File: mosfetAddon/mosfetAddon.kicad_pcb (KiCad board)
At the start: 2 copper layers, 89 x 61 mm, 70 parts, among them J1 coil, J10 Conn_01x18_Male, J2 coil, J3 coil, J4 coil, J5 coil, J6 coil, J7 coil, J8 coil, J9 pow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

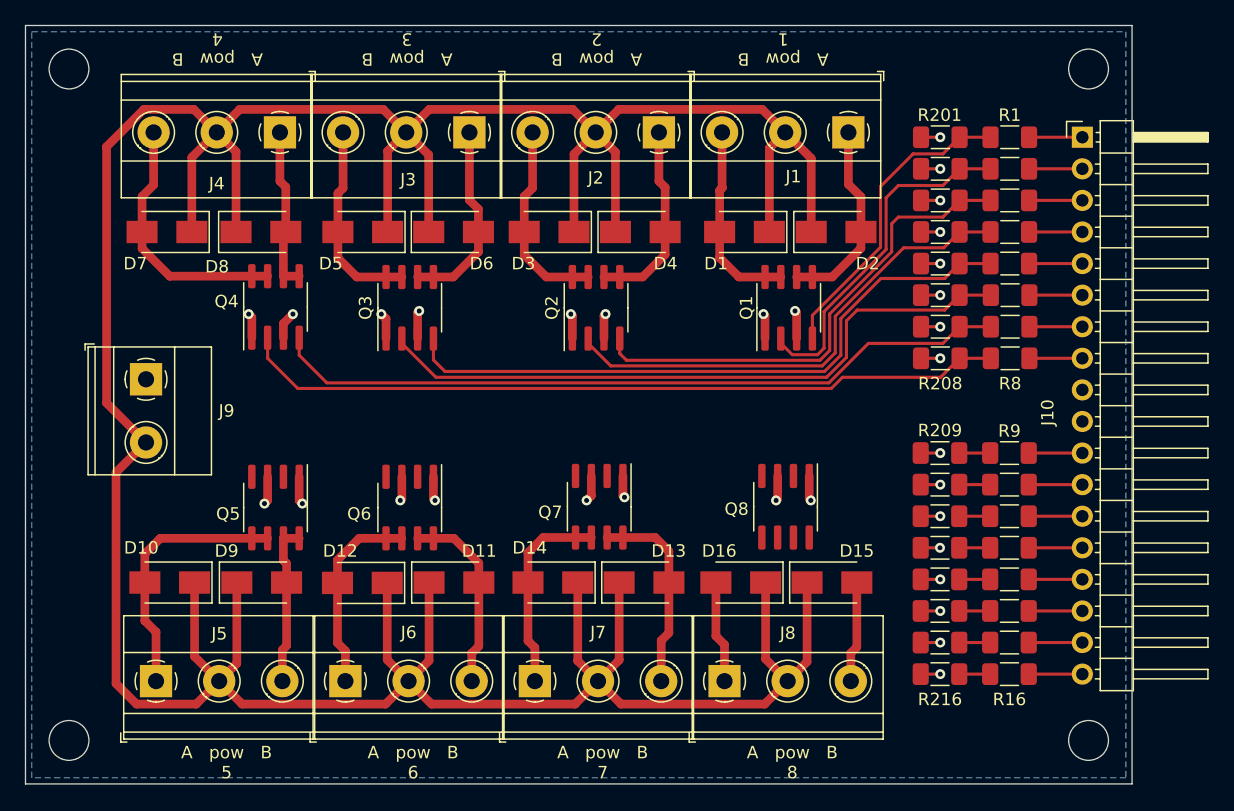
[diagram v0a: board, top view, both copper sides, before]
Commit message: relay are working but one. Multimaus control with IO sometimes seem buggy, but works in general. In worst case you have to press the same button another time.
Storing and saving program also works. Only the channel selection does not seem to work properly.
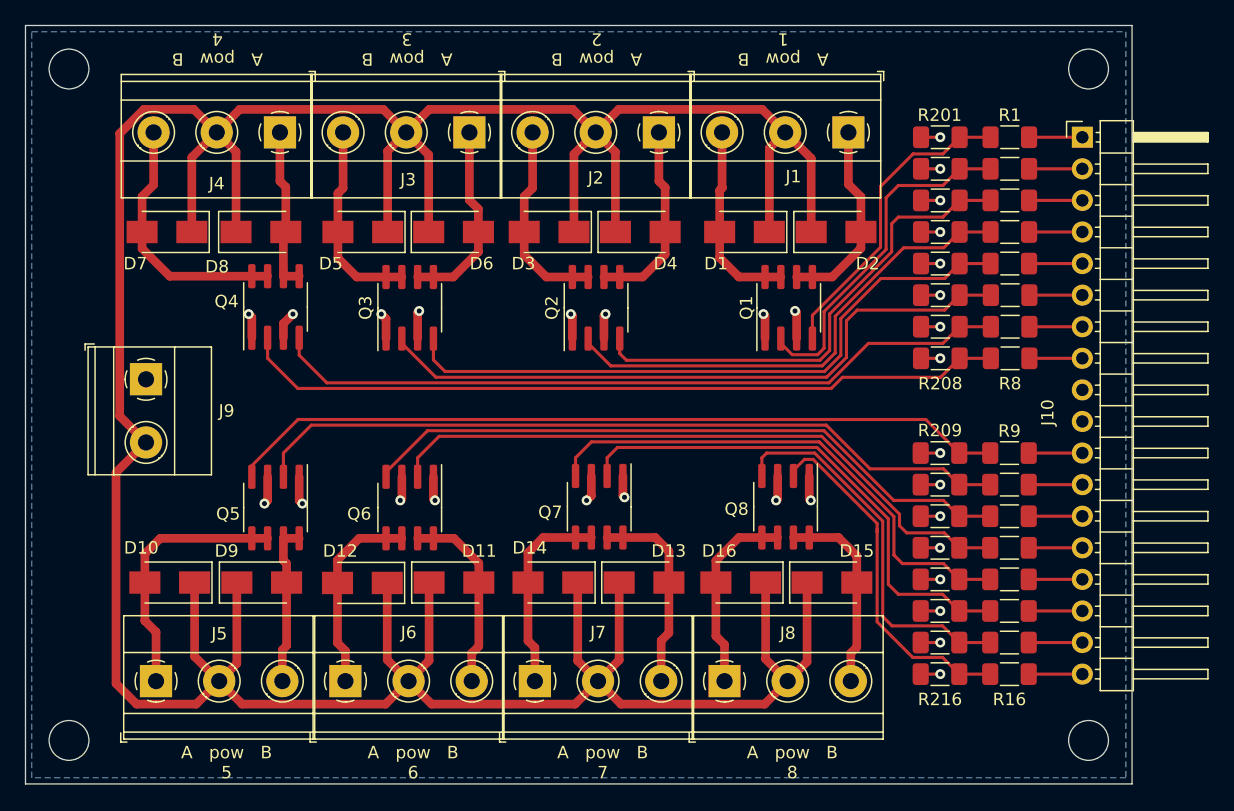
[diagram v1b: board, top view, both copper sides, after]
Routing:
- net Net-(Q5-Pad4): track 2.49 -> 62.9 mm
- net Net-(Q5-Pad2): track 2.49 -> 61.7 mm
- net Net-(Q6-Pad4): track 2.49 -> 53.2 mm
- net Net-(Q6-Pad2): track 2.49 -> 52.6 mm
- net Net-(Q7-Pad4): track 2.49 -> 41.7 mm
- net Net-(Q7-Pad2): track 2.49 -> 41.1 mm
- net Net-(Q8-Pad4): track 2.49 -> 30.8 mm
- net Net-(Q8-Pad2): track 2.49 -> 28.7 mm
- net coil8L: track 8.13 -> 16.0 mm
- net coil8R: track 8.22 -> 15.7 mm
- net pow: track 305.4 -> 304.5 mm

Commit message: about to make new branch for control panel usage
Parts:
- added D17: D_Bridge_+-AA, Diode_SMD:Diode_Bridge_Diotec_SO-DIL-Slim, F.Cu at (97.4, 110.9)
- added Q10: AO3400A, Package_TO_SOT_SMD:SOT-23, F.Cu at (106.0, 125.7)
- added Q11: AO3400A, Package_TO_SOT_SMD:SOT-23, F.Cu at (123.6, 125.7)
- added Q12: AO3400A, Package_TO_SOT_SMD:SOT-23, F.Cu at (118.6, 125.7)
- added Q13: AO3400A, Package_TO_SOT_SMD:SOT-23, F.Cu at (138.8, 125.6)
- added Q14: AO3400A, Package_TO_SOT_SMD:SOT-23, F.Cu at (134.1, 125.6)
- added Q15: AO3400A, Package_TO_SOT_SMD:SOT-23, F.Cu at (154.1, 125.6)
- added Q16: AO3400A, Package_TO_SOT_SMD:SOT-23, F.Cu at (149.1, 125.6)
- added Q9: AO3400A, Package_TO_SOT_SMD:SOT-23, F.Cu at (110.7, 125.7)
- Q1, Q2, Q3, Q4, Q5, Q6, Q7, Q8: value FDS6890A -> AO3400A; footprint Package_SO:SOIC-8_3.9x4.9mm_P1.27mm -> Package_TO_SOT_SMD:SOT-23
- moved Q8 44.0 mm to (110.7, 106.7), turned to 90 degrees
- moved Q7 35.0 mm to (105.8, 106.7), turned to 90 degrees
- moved Q4 28.6 mm to (138.7, 106.7)
- moved Q5 19.3 mm to (118.3, 106.7), turned to 90 degrees
- moved Q6 17.8 mm to (123.3, 106.7), turned to 90 degrees
- moved Q2 16.1 mm to (151.9, 106.6)
- moved Q3 12.9 mm to (133.7, 106.7)
- moved J9 6.92 mm to (95.2, 119.3)
- moved Q1 4.26 mm to (147.4, 106.6)
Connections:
- J9 pad 1: GND -> Net-(J9-Pad1)
- J9 pad 2: pow -> Net-(J9-Pad2)
- Q1 pad 1: GND -> Net-(R2-Pad2)
- Q1 pad 2: Net-(Q1-Pad2) -> GND
- Q1 pad 3: GND -> coil1L
- Q2 pad 1: GND -> Net-(Q2-Pad1)
- Q2 pad 2: Net-(Q2-Pad2) -> GND
- Q2 pad 3: GND -> coil1R
- Q3 pad 1: GND -> Net-(R204-Pad2)
- Q3 pad 2: Net-(Q3-Pad2) -> GND
- Q3 pad 3: GND -> coil2L
- Q4 pad 1: GND -> Net-(R203-Pad2)
- Q4 pad 2: Net-(Q4-Pad2) -> GND
- Q4 pad 3: GND -> coil2R
- Q5 pad 1: GND -> Net-(R206-Pad2)
- Q5 pad 2: Net-(Q5-Pad2) -> GND
- Q5 pad 3: GND -> coil3L
- Q6 pad 1: GND -> Net-(R205-Pad2)
- Q6 pad 2: Net-(Q6-Pad2) -> GND
- Q6 pad 3: GND -> coil3R
- Q7 pad 1: GND -> Net-(R208-Pad2)
- Q7 pad 2: Net-(Q7-Pad2) -> GND
- Q7 pad 3: GND -> coil4L
- Q8 pad 1: GND -> Net-(R207-Pad2)
- Q8 pad 2: Net-(Q8-Pad2) -> GND
- Q8 pad 3: GND -> coil4R
- R1 pad 2: Net-(Q1-Pad4) -> Net-(Q2-Pad1)
- R10 pad 2: Net-(Q5-Pad2) -> Net-(R210-Pad2)
- R11 pad 2: Net-(Q6-Pad4) -> Net-(R211-Pad2)
- R12 pad 2: Net-(Q6-Pad2) -> Net-(R212-Pad2)
- R13 pad 2: Net-(Q7-Pad4) -> Net-(R213-Pad2)
- R14 pad 2: Net-(Q7-Pad2) -> Net-(R214-Pad2)
- R15 pad 2: Net-(Q8-Pad4) -> Net-(R215-Pad2)
- R16 pad 2: Net-(Q8-Pad2) -> Net-(R216-Pad2)
- R2 pad 2: Net-(Q1-Pad2) -> Net-(R2-Pad2)
- R201 pad 2: Net-(Q1-Pad4) -> Net-(Q2-Pad1)
- R202 pad 2: Net-(Q1-Pad2) -> Net-(R2-Pad2)
- R203 pad 2: Net-(Q2-Pad4) -> Net-(R203-Pad2)
- R204 pad 2: Net-(Q2-Pad2) -> Net-(R204-Pad2)
- R205 pad 2: Net-(Q3-Pad4) -> Net-(R205-Pad2)
- R206 pad 2: Net-(Q3-Pad2) -> Net-(R206-Pad2)
- R207 pad 2: Net-(Q4-Pad4) -> Net-(R207-Pad2)
- R208 pad 2: Net-(Q4-Pad2) -> Net-(R208-Pad2)
- R209 pad 2: Net-(Q5-Pad4) -> Net-(R209-Pad2)
- R210 pad 2: Net-(Q5-Pad2) -> Net-(R210-Pad2)
- R211 pad 2: Net-(Q6-Pad4) -> Net-(R211-Pad2)
- R212 pad 2: Net-(Q6-Pad2) -> Net-(R212-Pad2)
- R213 pad 2: Net-(Q7-Pad4) -> Net-(R213-Pad2)
- R214 pad 2: Net-(Q7-Pad2) -> Net-(R214-Pad2)
- R215 pad 2: Net-(Q8-Pad4) -> Net-(R215-Pad2)
- R216 pad 2: Net-(Q8-Pad2) -> Net-(R216-Pad2)
- R3 pad 2: Net-(Q2-Pad4) -> Net-(R203-Pad2)
- R4 pad 2: Net-(Q2-Pad2) -> Net-(R204-Pad2)
- R5 pad 2: Net-(Q3-Pad4) -> Net-(R205-Pad2)
- R6 pad 2: Net-(Q3-Pad2) -> Net-(R206-Pad2)
- R7 pad 2: Net-(Q4-Pad4) -> Net-(R207-Pad2)
- R8 pad 2: Net-(Q4-Pad2) -> Net-(R208-Pad2)
- R9 pad 2: Net-(Q5-Pad4) -> Net-(R209-Pad2)
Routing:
- net Net-(R208-Pad2): track 0.00 -> 68.1 mm
- net Net-(R209-Pad2): track 0.00 -> 67.5 mm
- net Net-(R207-Pad2): track 0.00 -> 64.4 mm
- net Net-(R210-Pad2): track 0.00 -> 64.3 mm
- net Net-(Q5-Pad4): track 62.9 -> 0.00 mm
- net Net-(Q4-Pad2): track 61.8 -> 0.00 mm
- net Net-(Q5-Pad2): track 61.7 -> 0.00 mm
- net Net-(R206-Pad2): track 0.00 -> 59.9 mm
- net Net-(Q4-Pad4): track 59.8 -> 0.00 mm
- net Net-(R205-Pad2): track 0.00 -> 56.1 mm
- net Net-(R211-Pad2): track 0.00 -> 56.0 mm
- net Net-(Q3-Pad2): track 53.3 -> 0.00 mm
- net Net-(Q6-Pad4): track 53.2 -> 0.00 mm
- net Net-(Q6-Pad2): track 52.6 -> 0.00 mm
- net Net-(Q3-Pad4): track 52.2 -> 0.00 mm
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- added copper zone on F.Cu, net GND
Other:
- board text added: "POWER AC/DC"
- board text added: "Solenoid Unit By Bas Knippels"
